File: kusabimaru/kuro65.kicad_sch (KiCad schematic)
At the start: 28 parts, among them IC1 ATMEGA32U4, IC2 ATMEGA32U4, J1 ISP, J2 USB TYPE-C-31-M-12, SW1 SW_RESET, Y1 16MHz

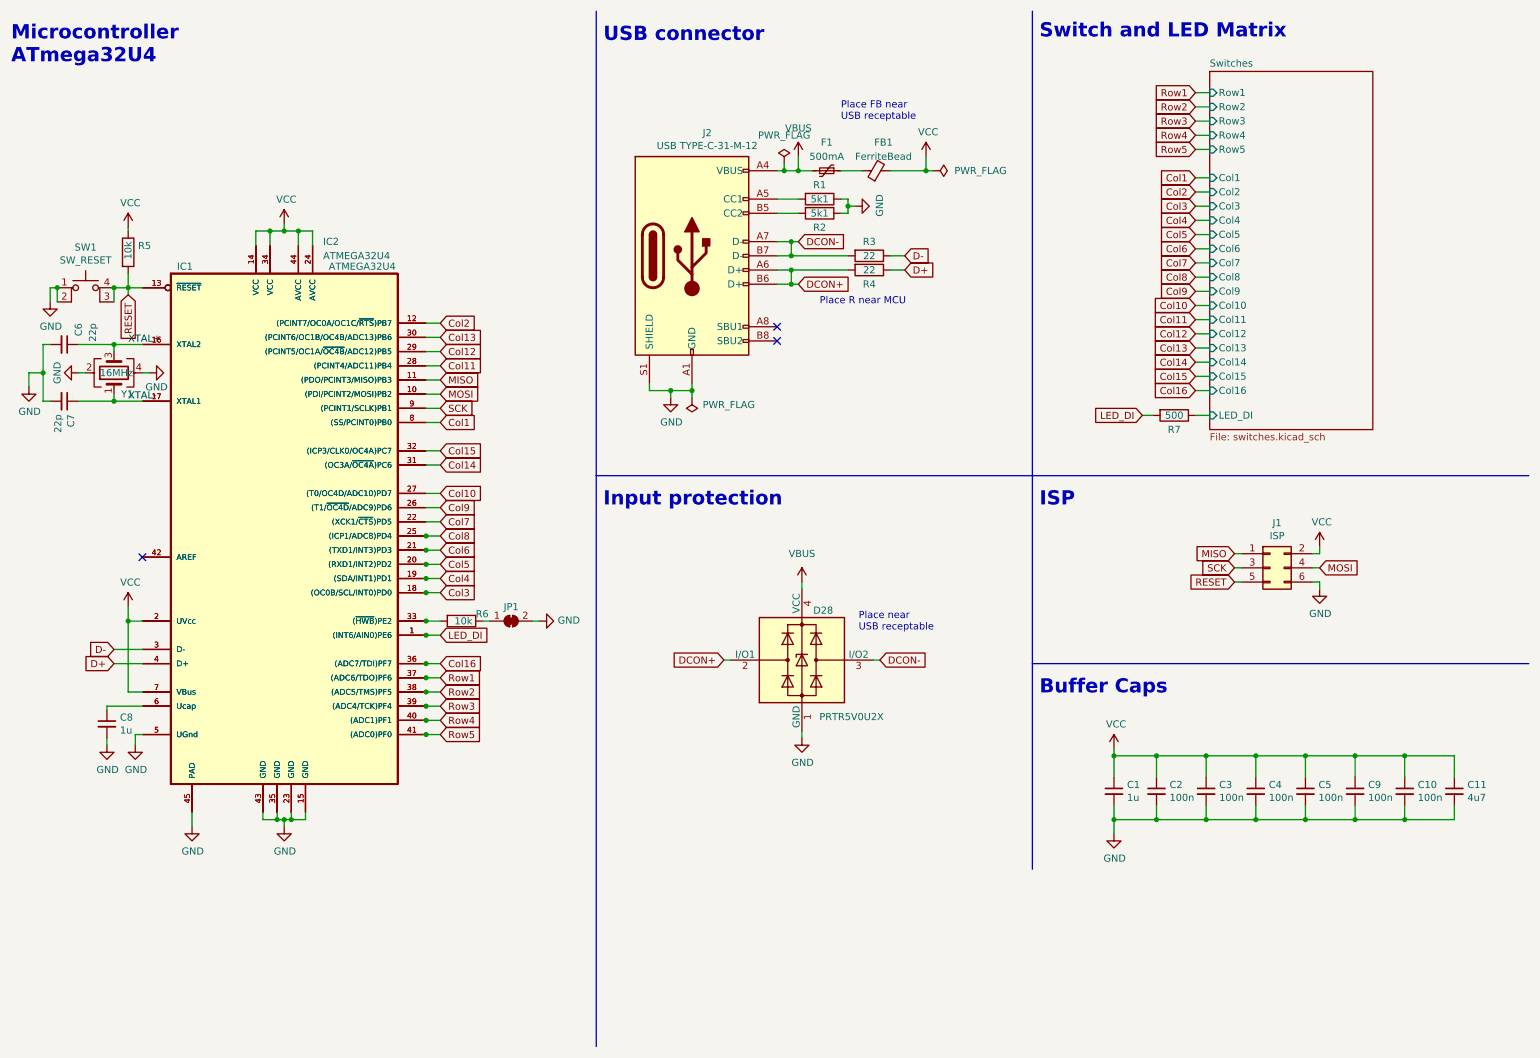
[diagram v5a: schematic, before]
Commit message: Updates to the PCB and the schematic.
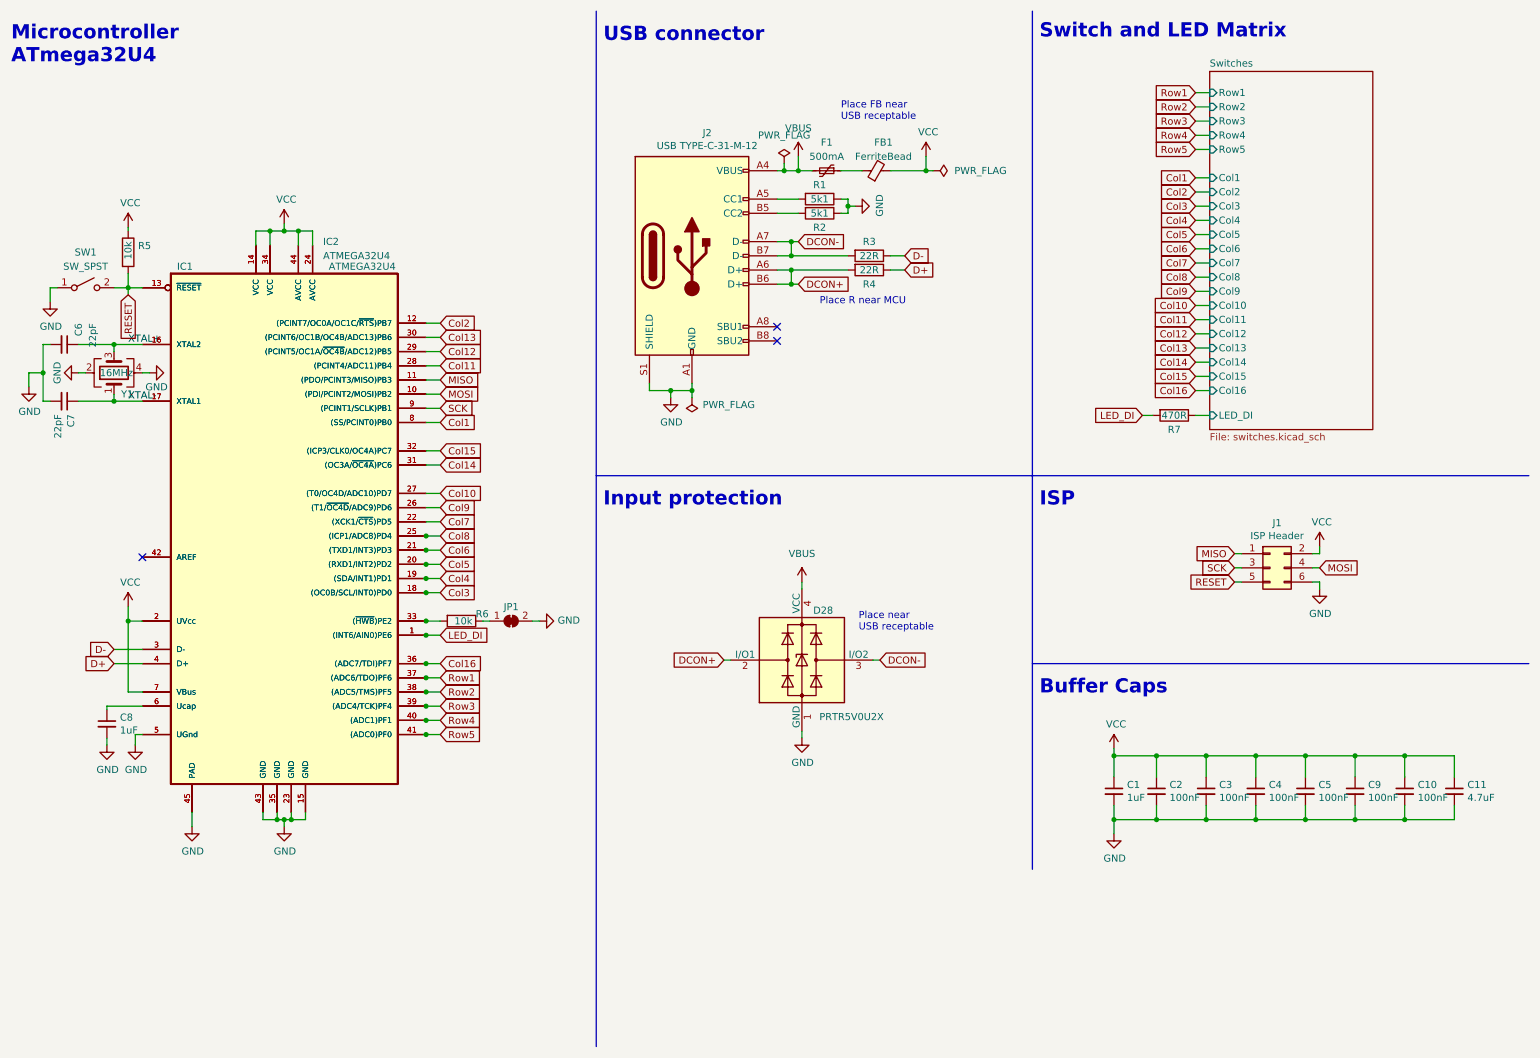
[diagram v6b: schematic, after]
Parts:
- removed SW1: SW_RESET, Button_Switch_SMD:SW_SPST_Omron_B3FS-100xP, symbol Switch:SW_MEC_5E
- added SW1: SW_SPST, Button_Switch_SMD:SW_SPST_TL3342, symbol Switch:SW_SPST
- C1, C8: value 1u -> 1uF; LCSC (none) -> C15849; Shop-URL (none) -> https://jlcpcb.com/partdetail/16531-CL10A105KB8NNNC/C15849
- C10, C2, C3, C4, C5, C9: value 100n -> 100nF; LCSC (none) -> C14663; Shop-URL (none) -> https://jlcpcb.com/partdetail/Yageo-CC0603KRX7R9BB104/C14663
- C11: value 4u7 -> 4.7uF; LCSC (none) -> C19666; Shop-URL (none) -> https://jlcpcb.com/partdetail/20375-CL10A475KO8NNNC/C19666
- C6, C7: value 22p -> 22pF; LCSC (none) -> C1653; Shop-URL (none) -> https://jlcpcb.com/partdetail/2005-CL10C220JB8NNNC/C1653
- D28: LCSC (none) -> C2827688; Shop-URL (none) -> https://jlcpcb.com/partdetail/TechPublic-PRTR5V0U2X/C2827688
- IC1: LCSC (none) -> C112161; Shop-URL (none) -> https://jlcpcb.com/partdetail/MicrochipTech-ATMEGA32U4MU/C1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
- J1: value ISP -> ISP Header
- J2: LCSC (none) -> C165948
- R1, R2: LCSC (none) -> C23186; Shop-URL (none) -> https://jlcpcb.com/partdetail/23913-0603WAF5101T5E/C23186
- R3, R4: value 22 -> 22R; LCSC (none) -> C23345; Shop-URL (none) -> https://jlcpcb.com/partdetail/24078-0603WAF220JT5E/C23345
- R5, R6: LCSC (none) -> C25804; Shop-URL (none) -> https://jlcpcb.com/partdetail/26547-0603WAF1002T5E/C25804
- R7: value 500 -> 470R; LCSC (none) -> C23179; Shop-URL (none) -> https://jlcpcb.com/partdetail/23906-0603WAF4700T5E/C23179
- Y1: LCSC (none) -> C13738; Shop-URL (none) -> https://jlcpcb.com/partdetail/YangxingTech-X322516MLB4SI/C1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
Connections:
- net GND: now also SW1.1 (A)
- net RESET: now also SW1.2 (B)

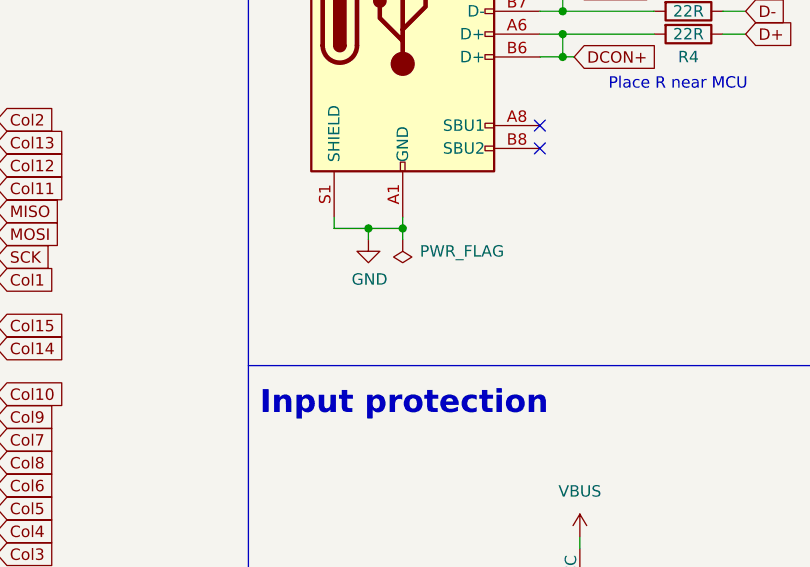
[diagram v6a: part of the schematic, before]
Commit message: Added USB shield circuit to schematic and PCB.
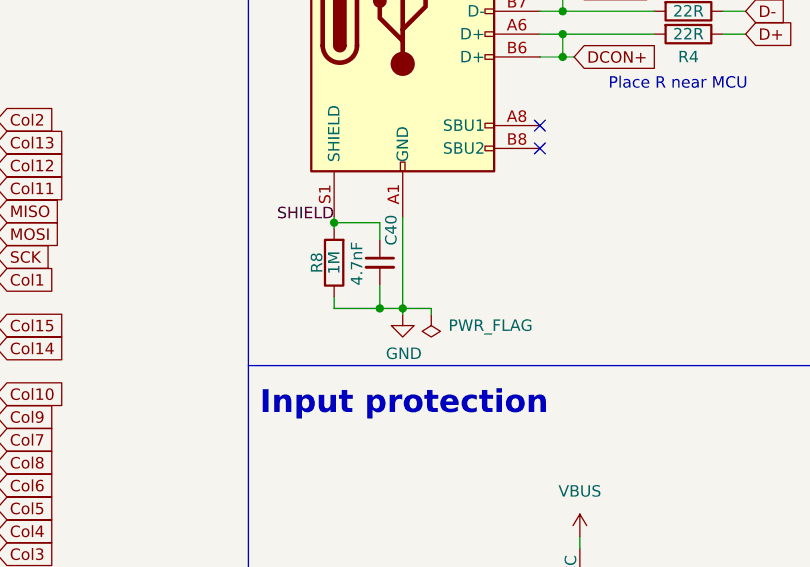
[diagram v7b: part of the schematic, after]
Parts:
- added C40: 4.7nF, Capacitor_SMD:C_0603_1608Metric_Pad1.08x0.95mm_HandSolder, symbol Device:C_Small
- added R8: 1M, Resistor_SMD:R_0603_1608Metric_Pad0.98x0.95mm_HandSolder, symbol Device:R
- F1: LCSC (none) -> C2844464; Shop-URL (none) -> https://jlcpcb.com/partdetail/Bhfuse-BSMD0603_05012V/C28444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
- FB1: LCSC (none) -> C307776; Shop-URL (none) -> https://jlcpcb.com/partdetail/Tdk-MPZ2012S101ATD25/C307776
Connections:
- net GND: now also C40.2, R8.1; no longer J2.S1 (SHIELD)
- new net SHIELD: C40.1, J2.S1 (SHIELD), R8.2

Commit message: Updated routing of USB traces.
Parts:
- D28: footprint Package_TO_SOT_SMD:SOT-143 -> random-keyboard-parts:SOT143B
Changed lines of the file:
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@@
     (property "Reference" "D28" (id 0) (at 158.75 119.38 0))
     (property "Value" "PRTR5V0U2X" (id 1) (at 163.83 138.43 0))
-    (property "Footprint" "Package_TO_SOT_SMD:SOT-143" (id 2) (at 156.464 128.27 0)
+    (property "Footprint" "random-keyboard-parts:SOT143B" (id 2) (at 156.464 128.27 0)
       (effects (font (size 1.27 1.27)) hide)
     )
@@
     )
     (path "/daa0536b-64b4-4f6e-bae2-f87779b0ee44"
-      (reference "D28") (unit 1) (value "PRTR5V0U2X") (footprint "Package_TO_SOT_SMD:SOT-143")
+      (reference "D28") (unit 1) (value "PRTR5V0U2X") (footprint "random-keyboard-parts:SOT143B")
     )
     (path "/00000000-0000-0000-0000-000060130ae4/00000000-0000-0000-0000-00006014f15f"
